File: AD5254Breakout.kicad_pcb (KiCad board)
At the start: 2 copper layers, 20.6 x 18 mm, 13 parts, among them J1 Conn_01x08, J2 Conn_01x08, U1 AD5254

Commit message: Correct line arround jumper
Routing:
- net Net-(JP8-Pad1): track 5.44 -> 5.99 mm
- net Net-(JP7-Pad1): track 5.40 -> 5.94 mm
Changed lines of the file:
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@@
     (thickness 1.6)
     (drawings 48)
-    (tracks 163)
+    (tracks 165)
     (zones 0)
     (modules 13)
@@
   (segment (start 168.0947 67.7774) (end 168.0947 67.41) (width 0.25) (layer F.Cu) (net 20))
   (segment (start 168.76 76.12) (end 168.76 76.2387) (width 0.25) (layer F.Cu) (net 21))
-  (segment (start 168.76 76.2387) (end 167.7986 77.2001) (width 0.25) (layer F.Cu) (net 21))
-  (segment (start 167.7986 77.2001) (end 166.4902 77.2001) (width 0.25) (layer F.Cu) (net 21))
-  (segment (start 166.4902 77.2001) (end 166.0402 76.7501) (width 0.25) (layer F.Cu) (net 21))
-  (segment (start 166.0402 76.7501) (end 164.1499 76.7501) (width 0.25) (layer F.Cu) (net 21))
-  (segment (start 164.1499 76.7501) (end 164.09 76.81) (width 0.25) (layer F.Cu) (net 21))
+  (segment (start 168.527492 77.2001) (end 168.76 76.967592) (width 0.25) (layer F.Cu) (net 21))
+  (segment (start 166.4902 77.2001) (end 168.527492 77.2001) (width 0.25) (layer F.Cu) (net 21))
+  (segment (start 168.76 76.967592) (end 168.76 76.12) (width 0.25) (layer F.Cu) (net 21))
+  (segment (start 166.0402 76.7501) (end 166.4902 77.2001) (width 0.25) (layer F.Cu) (net 21))
+  (segment (start 164.1499 76.7501) (end 166.0402 76.7501) (width 0.25) (layer F.Cu) (net 21))
+  (segment (start 164.09 76.81) (end 164.1499 76.7501) (width 0.25) (layer F.Cu) (net 21))
   (segment (start 168.75 73.86) (end 168.75 73.7295) (width 0.25) (layer F.Cu) (net 22))
-  (segment (start 168.75 73.7295) (end 167.541 72.5205) (width 0.25) (layer F.Cu) (net 22))
-  (segment (start 167.541 72.5205) (end 164.1845 72.5205) (width 0.25) (layer F.Cu) (net 22))
-  (segment (start 164.1845 72.5205) (end 164.01 72.695) (width 0.25) (layer F.Cu) (net 22))
+  (segment (start 168.75 73.012408) (end 168.75 73.86) (width 0.25) (layer F.Cu) (net 22))
+  (segment (start 168.258092 72.5205) (end 168.75 73.012408) (width 0.25) (layer F.Cu) (net 22))
+  (segment (start 164.1845 72.5205) (end 168.258092 72.5205) (width 0.25) (layer F.Cu) (net 22))
+  (segment (start 164.01 72.695) (end 164.1845 72.5205) (width 0.25) (layer F.Cu) (net 22))
   (zone (net 7) (net_name GND) (layer B.Cu) (hatch edge 0.508)
     (connect_pads (clearance 0.508))

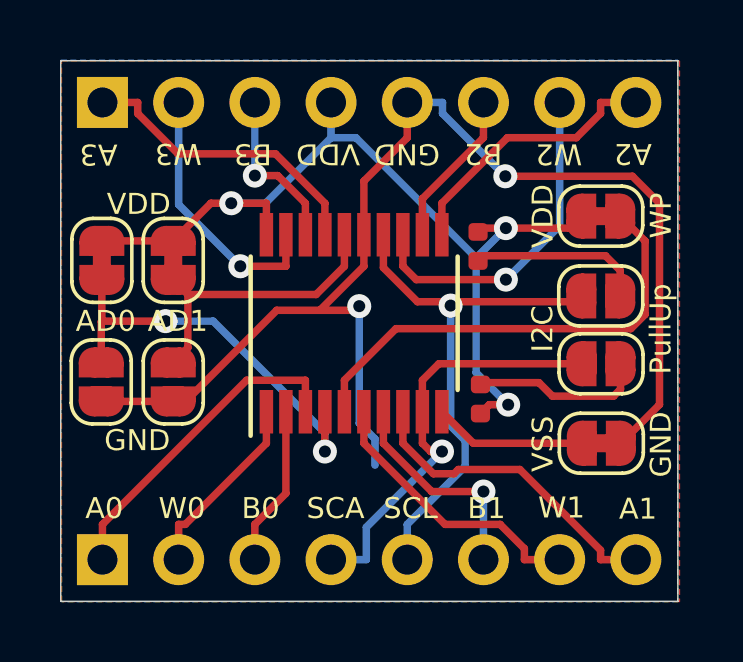
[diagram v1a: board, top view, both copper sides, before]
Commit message: Correct typo of text for SDA
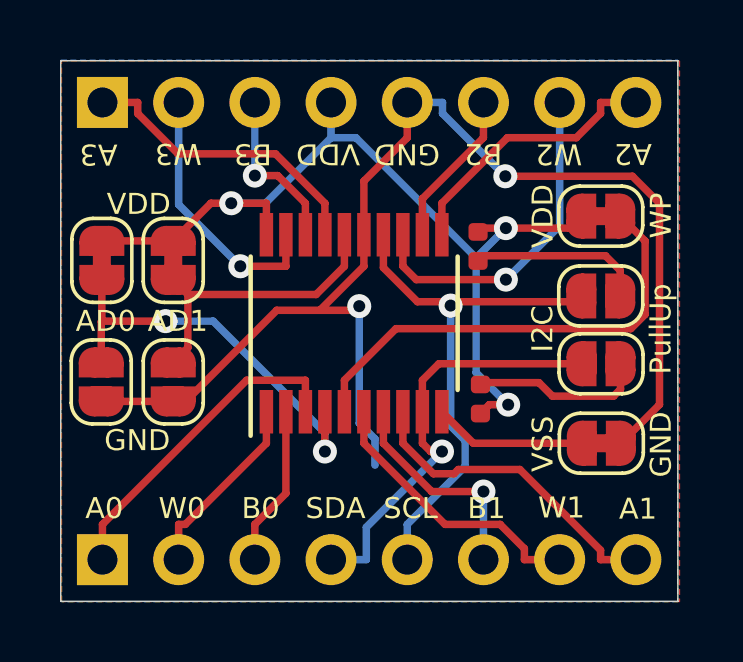
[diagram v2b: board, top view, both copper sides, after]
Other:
- board text removed: "SCA"
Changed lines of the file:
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@@
-(kicad_pcb (version 20171130) (host pcbnew 5.1.4-e60b266~84~ubuntu18.04.1)
+(kicad_pcb (version 20171130) (host pcbnew 5.1.5-52549c5~84~ubuntu18.04.1)
   (general
     (thickness 1.6)
@@
     (effects (font (size 0.7 0.7) (thickness 0.175)))
   )
-  (gr_text SCA (at 159.26 80.94) (layer F.SilkS)
+  (gr_text SDA (at 159.26 80.94) (layer F.SilkS)
     (effects (font (size 0.7 0.7) (thickness 0.175)))
   )
